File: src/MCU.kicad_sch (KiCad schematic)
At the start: 2 parts, among them J2 USB_B_Mini, U4 STM32F103CBT6

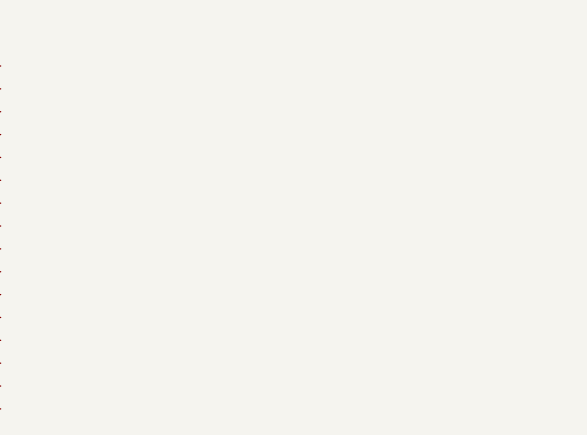
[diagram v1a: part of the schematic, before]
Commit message: switch USART1/USART2 as STM32F302RB w/ LQFP64 package does not have PD5/PD6 for bootloader on USART2
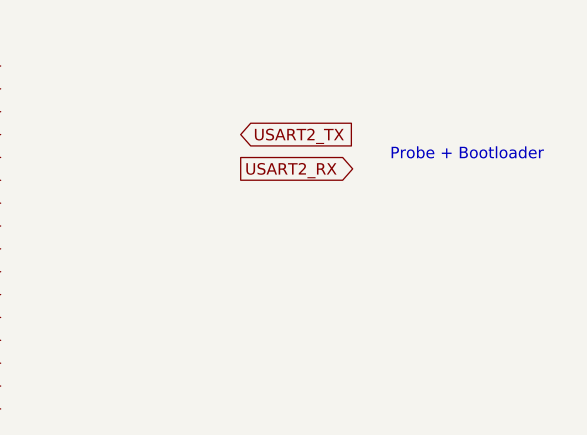
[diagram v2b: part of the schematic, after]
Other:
- note added: "Probe + Bootloader"
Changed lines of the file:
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@@
+		)
+	)
+	(text "Probe + Bootloader"
+		(exclude_from_sim no)
+		(at 131.826 39.116 0)
+		(effects
+			(font
+				(size 1.27 1.27)
+			)
+		)
+	)
+	(global_label "USART2_TX"
+		(shape input)
+		(at 106.68 36.83 0)
+		(fields_autoplaced yes)
+		(effects
+			(font
+				(size 1.27 1.27)
+			)
+			(justify left)
+		)
+		(property "Intersheetrefs" "${INTERSHEET_REFS}"
+			(at 119.8856 36.83 0)
+			(effects
+				(font
+					(size 1.27 1.27)
+				)
+				(justify left)
+				(hide yes)
+			)
+		)
+	)
+	(global_label "USART2_RX"
+		(shape output)
+		(at 106.68 40.64 0)
+		(fields_autoplaced yes)
+		(effects
+			(font
+				(size 1.27 1.27)
+			)
+			(justify left)
+		)
+		(property "Intersheetrefs" "${INTERSHEET_REFS}"
+			(at 120.188 40.64 0)
+			(effects
+				(font
+					(size 1.27 1.27)
+				)
+				(justify left)
+				(hide yes)
+			)
 		)
 	)
